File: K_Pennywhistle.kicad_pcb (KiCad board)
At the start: 2 copper layers, 80 x 100 mm, 66 parts, among them J1 Bias Control, J2 Conn_Coaxial, J3 P IN, J4 Conn_Coaxial, Q1 RD15HVF1, Q2 RD15HVF1, Q3 ZVP2106G, T1 BN43-302, T2 TLT BN43-202, T3 Output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

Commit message: first routed draft, fix some errors
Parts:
- added D1: D_TVS, Diode_SMD:D_0805_2012Metric, F.Cu at (153.2, 59.2)
- added D2: D_TVS, Diode_SMD:D_0805_2012Metric, F.Cu at (154.5, 100.2)
- moved C24 27.9 mm to (152.5, 120.0), turned to 0 degrees
- moved C1 23.0 mm to (155.0, 42.5), turned to 90 degrees
- moved C4 22.3 mm to (165.0, 42.5), turned to 90 degrees
- moved R10 18.0 mm to (115.0, 77.0)
- moved C3 16.0 mm to (145.0, 42.5), turned to 90 degrees
- moved R19 14.2 mm to (145.0, 130.0)
- moved Q3 13.9 mm to (145.0, 122.5)
- moved C2 13.2 mm to (135.0, 47.5), turned to 90 degrees
- moved R5 11.8 mm to (124.0, 62.0), turned to 180 degrees
- moved R9 11.4 mm to (115.0, 72.0)
- moved R6 11.2 mm to (124.0, 67.0), turned to 180 degrees
- moved L2 10.5 mm to (160.0, 42.4)
- moved L1 10.5 mm to (150.0, 42.5)
- moved C20 10.4 mm to (140.0, 125.0), turned to -90 degrees
- moved L3 10.1 mm to (172.5, 130.1)
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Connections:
- C15 pad 2: GND -> Net-(Q2-D)
- C18 pad 1: Net-(C14-Pad2) -> Net-(C18-Pad1)
- C19 pad 1: Net-(C14-Pad2) -> Net-(C18-Pad1)
- C22 pad 1: Net-(C22-Pad1) -> Net-(Q3-S)
- C24 pad 1: Net-(C22-Pad1) -> Net-(Q3-S)
- C25 pad 1: Net-(C22-Pad1) -> Net-(Q3-S)
- L4 pad 1: Net-(C22-Pad1) -> Net-(Q3-S)
- R12 pad 1: Net-(R12-Pad1) -> Net-(C14-Pad2)
- R13 pad 1: Net-(R12-Pad1) -> Net-(C14-Pad2)
- R15 pad 1: Net-(C14-Pad2) -> Net-(C18-Pad1)
- R15 pad 2: Net-(R12-Pad1) -> Net-(C14-Pad2)
- R16 pad 1: Net-(C14-Pad2) -> Net-(C18-Pad1)
- R16 pad 2: Net-(R12-Pad1) -> Net-(C14-Pad2)
- RV2 pad 2: Net-(C14-Pad2) -> Net-(C18-Pad1)
- T2 pad 1: Net-(T3-SC) -> Net-(T2-Pad1)
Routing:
- net Net-(C5-Pad1): track 0.00 -> 47.4 mm
- net Net-(Q3-S): track 0.00 -> 40.2 mm
- net Net-(T3-SC): track 0.00 -> 37.7 mm
- net Net-(U1-VO): track 0.00 -> 35.2 mm
- net Net-(C18-Pad1): track 0.00 -> 30.6 mm
- net Net-(C9-Pad2): track 0.00 -> 24.0 mm
- net Net-(C14-Pad2): track 0.00 -> 19.8 mm
- net Net-(U1-VI): track 0.00 -> 19.0 mm
- net +12V: track 0.00 -> 18.5 mm
- net Net-(C1-Pad1): track 0.00 -> 16.2 mm
- net Net-(C23-Pad1): track 0.00 -> 14.9 mm
- net Net-(J4-In): track 0.00 -> 14.4 mm
- net Net-(T1-AA): track 0.00 -> 14.1 mm
- net Net-(D2-A1): track 0.00 -> 9.17 mm
- net Net-(D1-A1): track 0.00 -> 7.87 mm
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
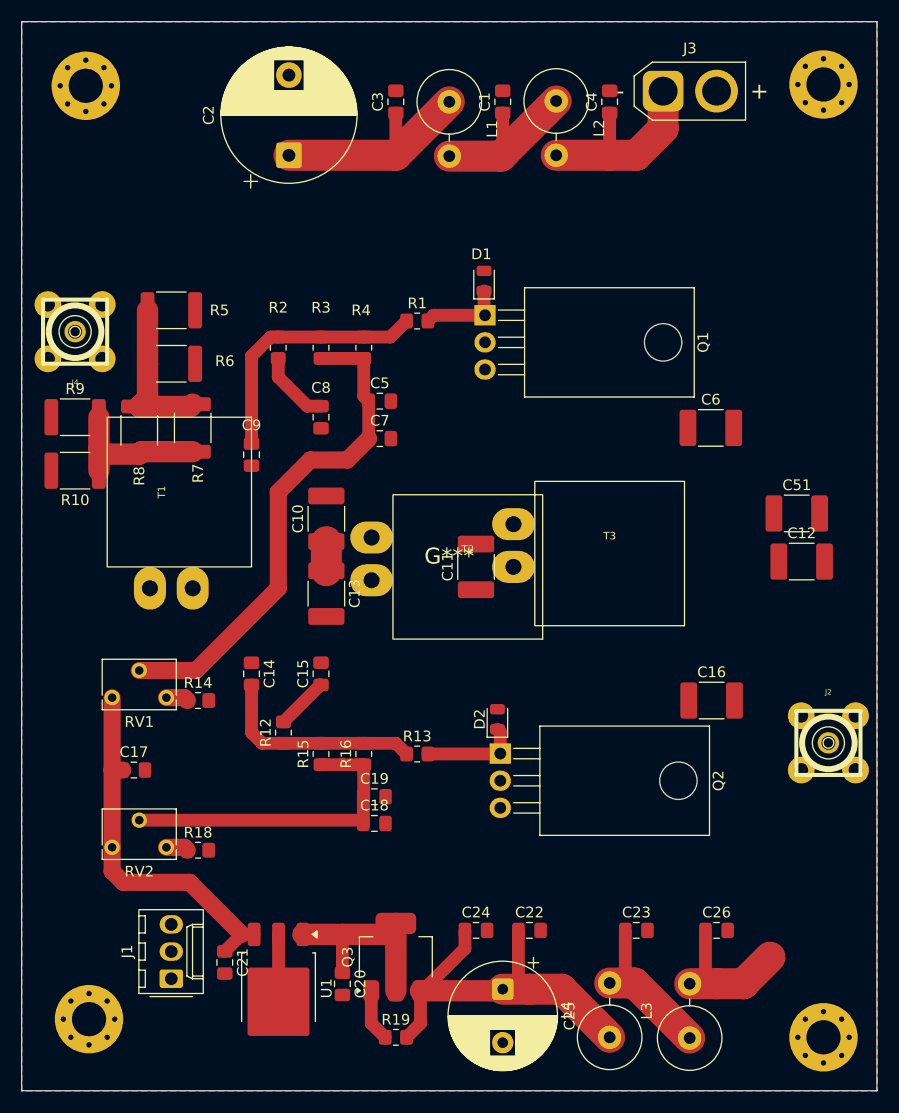
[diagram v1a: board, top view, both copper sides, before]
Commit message: near RTM, iBom and 3D image added
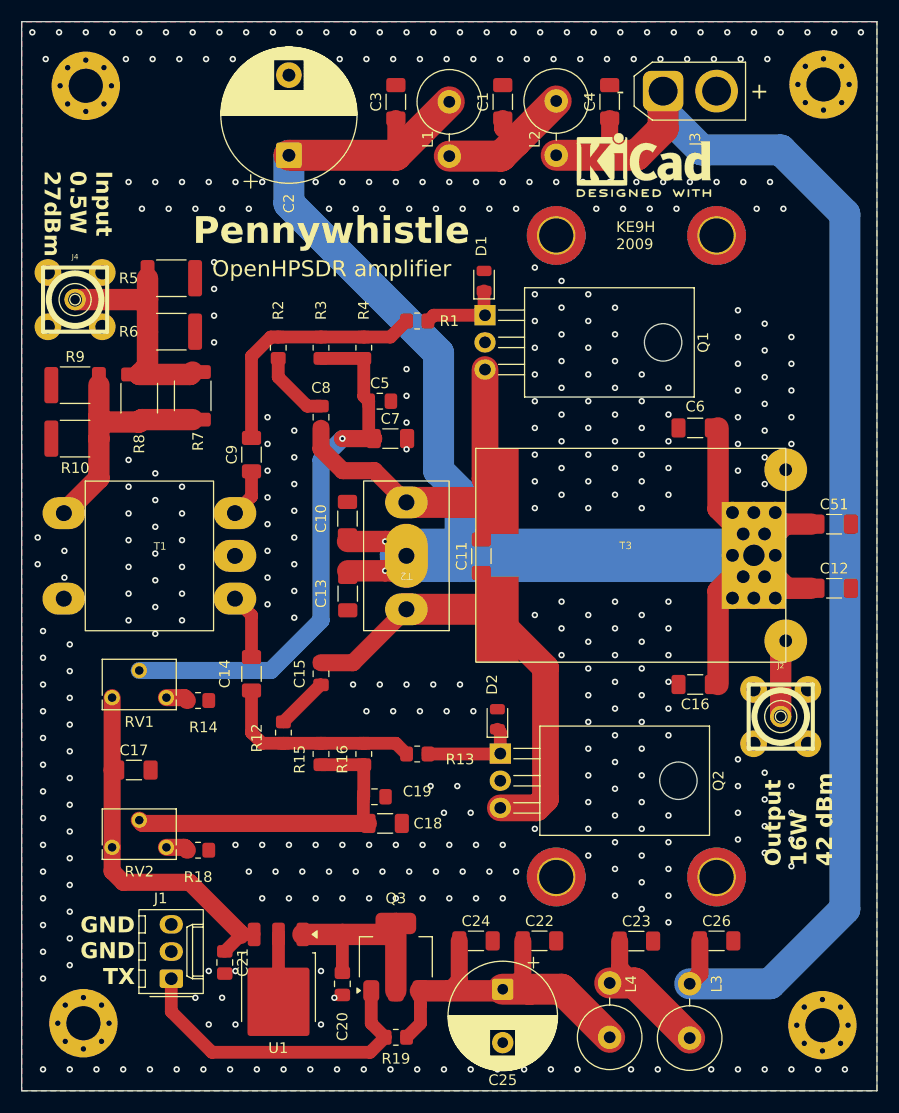
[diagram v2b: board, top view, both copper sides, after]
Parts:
- added H105: MountingHole_Pad, MountingHole:MountingHole_3.2mm_M3_ISO14580_Pad_TopBottom, F.Cu at (160.0, 55.0)
- added H106: MountingHole_Pad, MountingHole:MountingHole_3.2mm_M3_ISO14580_Pad_TopBottom, F.Cu at (175.0, 55.0)
- added H107: MountingHole_Pad, MountingHole:MountingHole_3.2mm_M3_ISO14580_Pad_TopBottom, F.Cu at (160.0, 115.0)
- added H108: MountingHole_Pad, MountingHole:MountingHole_3.2mm_M3_ISO14580_Pad_TopBottom, F.Cu at (175.0, 115.0)
- added REF**: KiCad-Logo2_5mm_SilkScreen, Symbol:KiCad-Logo2_5mm_SilkScreen, F.Cu at (168.2, 48.4)
- C1, C14, C17, C18, C22, C23, C24, C26, C3, C4, C7, C9: footprint Capacitor_SMD:C_0805_2012Metric_Pad1.18x1.45mm_HandSolder -> Capacitor_SMD:C_1206_3216Metric_Pad1.33x1.80mm_HandSolder
- C10, C11, C12, C13, C16, C51, C6: footprint Capacitor_SMD:C_1812_4532Metric_Pad1.57x3.40mm_HandSolder -> Capacitor_SMD:C_1206_3216Metric_Pad1.33x1.80mm_HandSolder
- J2: value Conn_Coaxial -> DMZ
- J4: value Conn_Coaxial -> SMA
- moved T1 6.06 mm to (123.0, 85.0), turned to 0 degrees
- moved T2 5.79 mm to (146.0, 86.0), turned to 180 degrees
- moved J2 5.09 mm to (181.0, 100.0)
- moved C12 3.93 mm to (186.0, 88.0)
- moved C51 3.64 mm to (186.0, 82.0)
- moved J4 3.00 mm to (115.0, 61.0)
- moved R10 3.00 mm to (115.0, 74.0)
- moved R5 3.00 mm to (124.0, 59.0)
- moved R6 3.00 mm to (124.0, 64.0)
- moved R7 3.00 mm to (126.0, 70.0)
- moved R8 3.00 mm to (121.0, 70.2)
- moved R9 3.00 mm to (115.0, 69.0)
- moved C16 2.15 mm to (173.0, 97.0), turned to 180 degrees
- moved C13 2.00 mm to (140.5, 88.5)
- moved C10 1.98 mm to (140.5, 81.5)
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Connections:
- C26 pad 1: Net-(T3-SC) -> +12V
- L3 pad 2: Net-(T3-SC) -> +12V
- T2 pad 1: Net-(T2-Pad1) -> Net-(T3-SC)
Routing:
- net +12V: track 18.5 -> 127.7 mm
- net Net-(T3-SC): track 37.7 -> 146.5 mm, vias 0 -> 2
- net Net-(Q2-D): track 0.00 -> 42.2 mm
- net Net-(Q1-D): track 0.00 -> 32.8 mm
- net Net-(J1-Pin_1): track 4.89 -> 30.1 mm
- net Net-(T1-AA): track 14.1 -> 22.4 mm
- net Net-(J2-In): track 0.00 -> 7.28 mm
- net Net-(J4-In): track 14.4 -> 21.2 mm
- net Net-(T1-SA): track 0.00 -> 6.11 mm
- net Net-(T1-SB): track 0.00 -> 4.55 mm
- net Net-(C5-Pad1): track 47.4 -> 51.6 mm, vias 0 -> 1
- net Net-(Q3-S): track 40.2 -> 38.3 mm
- net Net-(C1-Pad1): track 16.2 -> 15.0 mm
- net Net-(C18-Pad1): track 30.6 -> 31.3 mm
- net Net-(C9-Pad2): track 24.0 -> 23.5 mm
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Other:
- board text added: "GND GND TX"
- board text added: "Input 0.5W 27dBm"
- board text added: "KE9H 2009"
- board text added: "OpenHPSDR amplifier"
- board text added: "Output 16W 42 dBm"
- board text added: "Pennywhistle"

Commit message: RTM (at last!)
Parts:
- removed REF**: KiCad-Logo2_5mm_SilkScreen, Symbol:KiCad-Logo2_5mm_SilkScreen
- moved Q2 1.17 mm to (153.6, 103.6)
- moved D2 1.00 mm to (153.5, 100.2)
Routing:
- net Net-(Q2-D): track 42.2 -> 43.4 mm
- net Net-(D2-A1): track 9.17 -> 8.06 mm
- net GND: vias 387 -> 371
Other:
- outline, holes or cut-outs redrawn

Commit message: release, new Gerber, minor mods
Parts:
- moved C12 2.00 mm to (184.0, 88.0)
- moved C51 1.94 mm to (184.1, 82.0)
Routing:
- net Net-(T3-SC): track 146.5 -> 140.1 mm
- net GND: vias 371 -> 372
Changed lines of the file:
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@@
 			(plot_on_all_layers_selection 0x00000000_00000000_00000000_00000000)
 			(disableapertmacros no)
-			(usegerberextensions no)
+			(usegerberextensions yes)
 			(usegerberattributes yes)
 			(usegerberadvancedattributes yes)
-			(creategerberjobfile yes)
+			(creategerberjobfile no)
 			(dashed_line_dash_ratio 12)
 			(dashed_line_gap_ratio 3)
@@
 			(outputformat 1)
 			(mirror no)
-			(drillshape 1)
+			(drillshape 0)
 			(scaleselection 1)
-			(outputdirectory "")
+			(outputdirectory "Gerber/")
 		)
 	)
@@
 	(footprint "Capacitor_SMD:C_1206_3216Metric_Pad1.33x1.80mm_HandSolder"
 		(layer "F.Cu")
-		(at 186 82)
+		(at 184.0625 81.989913)
 		(descr "Capacitor SMD 1206 (3216 Metric), square (rectangular) end terminal, IPC-7351 nominal with elongated pad for handsoldering. (Body size source: IPC-SM-782 page 76, https://www.pcb-3d.com/wordpress/wp-content/uploads/ipc-sm-782a_amendment_1_and_2.pdf)")
 		(tags "capacitor handsolder")
@@
 			(layer "F.CrtYd")
 		)
-		(pad "1" thru_hole oval
+		(pad "1" smd oval
 			(at -9 -4)
 			(size 4 3)
-			(drill 1.5)
-			(layers "*.Cu" "*.Mask")
-			(remove_unused_layers no)
+			(layers "F.Cu" "F.Mask" "F.Paste")
 			(net "Net-(T1-AA)")
 			(pinfunction "AA_1")
 			(pintype "passive")
 		)
-		(pad "2" thru_hole oval
+		(pad "2" smd oval
 			(at -9.009242 4)
 			(size 4 3)
-			(drill 1.5)
-			(layers "*.Cu" "*.Mask")
-			(remove_unused_layers no)
+			(layers "F.Cu" "F.Mask" "F.Paste")
 			(net "GND")
 			(pinfunction "AB_2")
 			(pintype "passive")
 		)
-		(pad "3" thru_hole oval
+		(pad "3" smd oval
 			(at 7 4)
 			(size 4 3)
-			(drill 1.5)
-			(layers "*.Cu" "*.Mask")
-			(remove_unused_layers no)
+			(layers "F.Cu" "F.Mask" "F.Paste")
 			(net "Net-(T1-SA)")
 			(pinfunction "SA_3")
 			(pintype "passive")
 		)
-		(pad "4" thru_hole oval
+		(pad "4" smd oval
 			(at 7 0)
 			(size 4 3)
-			(drill 1.5)
-			(layers "*.Cu" "*.Mask")
-			(remove_unused_layers no)
+			(layers "F.Cu" "F.Mask" "F.Paste")
 			(net "GND")
 			(pinfunction "SC_4")
 			(pintype "passive")
 		)
-		(pad "5" thru_hole oval
+		(pad "5" smd oval
 			(at 7 -4)
 			(size 4 3)
-			(drill 1.5)
-			(layers "*.Cu" "*.Mask")
-			(remove_unused_layers no)
+			(layers "F.Cu" "F.Mask" "F.Paste")
 			(net "Net-(T1-SB)")
 			(pinfunction "SB_5")
@@
 	(footprint "Capacitor_SMD:C_1206_3216Metric_Pad1.33x1.80mm_HandSolder"
 		(layer "F.Cu")
-		(at 186 88)
+		(at 184 88)
 		(descr "Capacitor SMD 1206 (3216 Metric), square (rectangular) end terminal, IPC-7351 nominal with elongated pad for handsoldering. (Body size source: IPC-SM-782 page 76, https://www.pcb-3d.com/wordpress/wp-content/uploads/ipc-sm-782a_amendment_1_and_2.pdf)")
 		(tags "capacitor handsolder")
@@
 		(pad "1" thru_hole oval
 			(at 0 1 180)
-			(size 4 6)
+			(size 4 5)
 			(drill 1.5)
 			(layers "*.Cu" "*.Mask")
@@
 	)
 	(via
-		(at 160.5 94.25)
-		(size 0.6)
-		(drill 0.3)
-		(layers "F.Cu" "B.Cu")
-		(free yes)
-		(net "GND")
-	)
-	(via
 		(at 164.75 38.5)
 		(size 0.6)
@@
 	)
 	(via
+		(at 141 92)
+		(size 0.6)
+		(drill 0.3)
+		(layers "F.Cu" "B.Cu")
+		(free yes)
+		(net "GND")
+	)
+	(via
 		(at 112 107)
 		(size 0.6)
@@
 	)
 	(via
+		(at 139.7 99.5)
+		(size 0.6)
+		(drill 0.3)
+		(layers "F.Cu" "B.Cu")
+		(free yes)
+		(net "GND")
+	)
+	(via
 		(at 112 133)
 		(size 0.6)
@@
 	)
 	(segment
-		(start 144.589484 86.3625)
-		(end 145.988 84.963984)
-		(width 2)
+		(start 180.415859 81.989913)
+		(end 179.488606 82.917166)
+		(width 1.6)
 		(layer "F.Cu")
 		(net "Net-(T3-SC)")
 	)
 	(segment
-		(start 144.646508 83.622492)
+		(start 144.589484 86.3625)
 		(end 145.988 84.963984)
 		(width 2)
@@
 	)
 	(segment
-		(start 181.405772 82)
-		(end 178.488606 84.917166)
+		(start 144.646508 83.622492)
+		(end 145.988 84.963984)
 		(width 2)
 		(layer "F.Cu")
@@
 	)
 	(segment
-		(start 183.8625 88)
-		(end 181.57144 88)
-		(width 2)
+		(start 180.57144 88)
+		(end 179.488606 86.917166)
+		(width 1.6)
 		(layer "F.Cu")
 		(net "Net-(T3-SC)")
@@
 	)
 	(segment
-		(start 144 83.622492)
-		(end 144.646508 83.622492)
-		(width 2)
+		(start 182.4375 88)
+		(end 180.57144 88)
+		(width 1.6)
 		(layer "F.Cu")
 		(net "Net-(T3-SC)")
 	)
 	(segment
-		(start 140.5 86.3625)
-		(end 144 86.3625)
+		(start 144 83.622492)
+		(end 144.646508 83.622492)
 		(width 2)
 		(layer "F.Cu")
@@
 	)
 	(segment
-		(start 183.8625 82)
-		(end 181.405772 82)
+		(start 140.5 86.3625)
+		(end 144 86.3625)
 		(width 2)
 		(layer "F.Cu")
@@
 	)
 	(segment
-		(start 181.57144 88)
-		(end 178.488606 84.917166)
-		(width 2)
+		(start 182.5 81.989913)
+		(end 180.415859 81.989913)
+		(width 1.6)
 		(layer "F.Cu")
 		(net "Net-(T3-SC)")
@@
 	)
 	(zone
+		(layer "F.Cu")
+		(hatch edge 0.5)
+		(connect_pads
+			(clearance 0)
+		)
+		(min_thickness 0.25)
+		(keepout
+			(tracks allowed)
+			(vias allowed)
+			(pads allowed)
+			(copperpour not_allowed)
+			(footprints allowed)
+		)
+		(placement
+			(enabled no)
+			(sheetname "")
+		)
+		(fill
+			(thermal_gap 0.5)
+			(thermal_bridge_width 0.5)
+			(island_removal_mode 0)
+		)
+		(polygon
+			(pts
+				(xy 157 77) (xy 157 92) (xy 143 92) (xy 143 77)
+			)
+		)
+	)
+	(zone

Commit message: minor mods, new Gerber & iBom, schematic pdf,RTM
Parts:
- added REF**: KiCad-Logo2_5mm_SilkScreen, Symbol:KiCad-Logo2_5mm_SilkScreen, F.Cu at (168.0, 49.0)
- added REF**: OSHW-Logo_5.7x6mm_SilkScreen, Symbol:OSHW-Logo_5.7x6mm_SilkScreen, F.Cu at (123.0, 49.0)
